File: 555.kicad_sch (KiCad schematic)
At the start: 57 parts, among them J2 Screw_Terminal_01x02, P1 USB_C_Plug_USB2.0, SW1 SW_Push, SW2 SW_Push, SW3 SW_Push, SW4 SW_Push, SW5 SW_Push, SW6 SW_Push, SW7 SW_Push, SW8 SW_Push, U1 NE555P

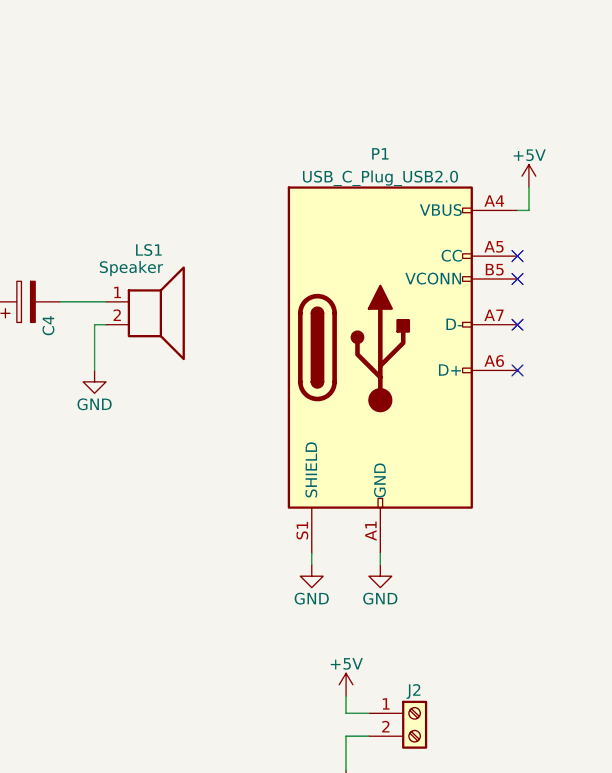
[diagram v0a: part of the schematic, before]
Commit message: USB-C resistor CC
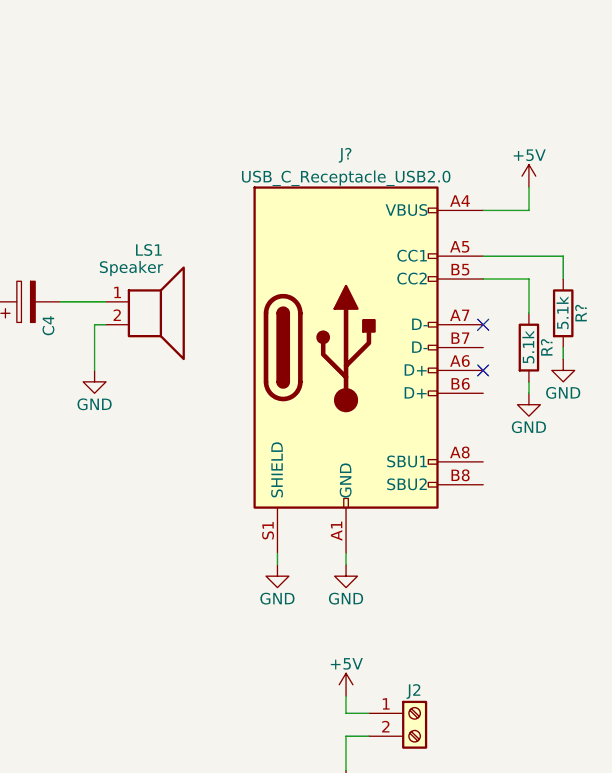
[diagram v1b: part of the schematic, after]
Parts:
- removed P1: USB_C_Plug_USB2.0, Connector_USB:USB_C_Receptacle_GCT_USB4085, symbol Connector:USB_C_Plug_USB2.0
- added J?: USB_C_Receptacle_USB2.0, symbol Connector:USB_C_Receptacle_USB2.0
- added R? (x2): 5.1k, Resistor_THT:R_Axial_DIN0207_L6.3mm_D2.5mm_P10.16mm_Horizontal, symbol Device:R
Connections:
- net +5V: now also J?.A4 (VBUS), J?.A9 (VBUS), J?.B4 (VBUS), J?.B9 (VBUS)
- net GND: now also J?.A1 (GND), J?.A12 (GND), J?.B1 (GND), J?.B12 (GND), J?.S1 (SHIELD), R?.2, R?.2
- new net: J?.B5 (CC2), R?.1
- new net: J?.A5 (CC1), R?.1
- no-connect marks 4 -> 2

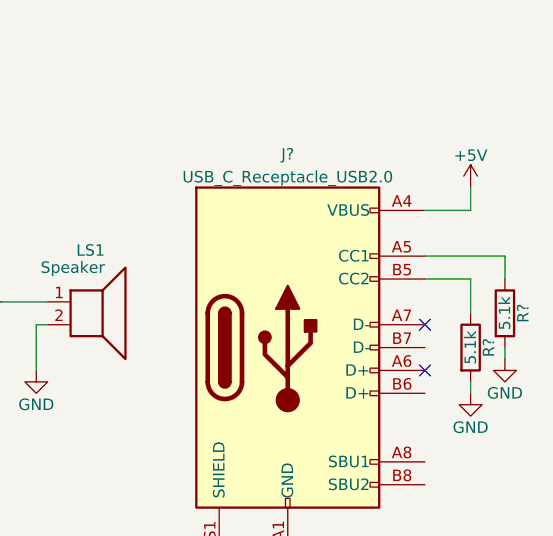
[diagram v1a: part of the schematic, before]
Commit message: USB-C resistor CC
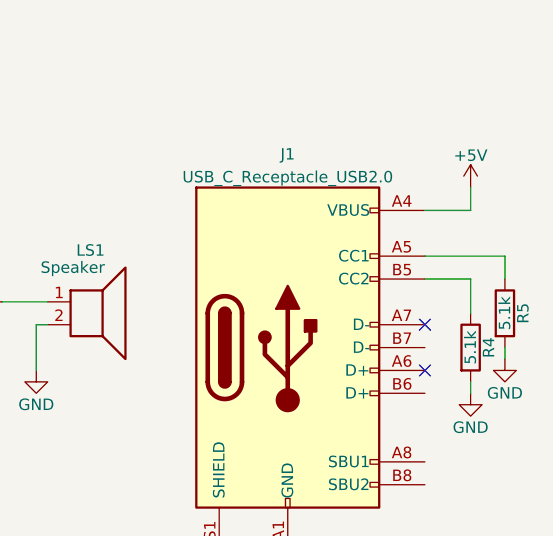
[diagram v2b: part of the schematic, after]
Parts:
- J1: renamed from J?; footprint (none) -> Connector_USB:USB_C_Receptacle_GCT_USB4085
- gave numbers to parts that had none: 2
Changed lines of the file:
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@@
   (symbol (lib_id "Device:R") (at 278.13 97.79 0) (unit 1)
     (in_bom yes) (on_board yes)
-    (property "Reference" "R?" (id 0) (at 280.162 97.79 90))
+    (property "Reference" "R4" (id 0) (at 280.162 97.79 90))
     (property "Value" "5.1k" (id 1) (at 278.13 97.79 90))
     (property "Footprint" "Resistor_THT:R_Axial_DIN0207_L6.3mm_D2.5mm_P10.16mm_Horizontal" (id 2) (at 276.352 97.79 90)
@@
   (symbol (lib_id "Device:R") (at 281.94 93.98 0) (unit 1)
     (in_bom yes) (on_board yes)
-    (property "Reference" "R?" (id 0) (at 283.972 93.98 90))
+    (property "Reference" "R5" (id 0) (at 283.972 93.98 90))
     (property "Value" "5.1k" (id 1) (at 281.94 93.98 90))
     (property "Footprint" "Resistor_THT:R_Axial_DIN0207_L6.3mm_D2.5mm_P10.16mm_Horizontal" (id 2) (at 280.162 93.98 90)
@@
   (symbol (lib_id "power:GND") (at 281.94 99.06 0) (unit 1)
     (in_bom yes) (on_board yes)
-    (property "Reference" "#PWR?" (id 0) (at 281.94 105.41 0)
+    (property "Reference" "#PWR0105" (id 0) (at 281.94 105.41 0)
       (effects (font (size 1.27 1.27)) hide)
     )
@@
   (symbol (lib_id "power:GND") (at 278.13 102.87 0) (unit 1)
     (in_bom yes) (on_board yes)
-    (property "Reference" "#PWR?" (id 0) (at 278.13 109.22 0)
+    (property "Reference" "#PWR0104" (id 0) (at 278.13 109.22 0)
       (effects (font (size 1.27 1.27)) hide)
     )
@@
   (symbol (lib_id "Connector:USB_C_Receptacle_USB2.0") (at 257.81 97.79 0) (unit 1)
     (in_bom yes) (on_board yes) (fields_autoplaced)
-    (property "Reference" "J?" (id 0) (at 257.81 76.3102 0))
+    (property "Reference" "J1" (id 0) (at 257.81 76.3102 0))
     (property "Value" "USB_C_Receptacle_USB2.0" (id 1) (at 257.81 78.8471 0))
-    (property "Footprint" "" (id 2) (at 261.62 97.79 0)
+    (property "Footprint" "Connector_USB:USB_C_Receptacle_GCT_USB4085" (id 2) (at 261.62 97.79 0)
       (effects (font (size 1.27 1.27)) hide)
     )
@@
       (reference "#PWR0103") (unit 1) (value "GND") (footprint "")
     )
+    (path "/b2e6477c-ad92-49a7-aece-eea1bc30ca39"
+      (reference "#PWR0104") (unit 1) (value "GND") (footprint "")
+    )
+    (path "/7a7afcf7-9c2f-4d82-ae0b-cb669e335a64"
+      (reference "#PWR0105") (unit 1) (value "GND") (footprint "")
+    )
     (path "/43a05453-035c-453b-be11-f0c5789d3e42"
       (reference "#PWR0106") (unit 1) (value "GND") (footprint "")
@@
       (reference "#PWR0108") (unit 1) (value "+5V") (footprint "")
     )
-    (path "/7a7afcf7-9c2f-4d82-ae0b-cb669e335a64"
-      (reference "#PWR?") (unit 1) (value "GND") (footprint "")
-    )
-    (path "/b2e6477c-ad92-49a7-aece-eea1bc30ca39"
-      (reference "#PWR?") (unit 1) (value "GND") (footprint "")
-    )
     (path "/f94bea49-4652-41d4-bccc-fb87f892bbde"
       (reference "C1") (unit 1) (value "10uF") (footprint "Capacitor_THT:CP_Radial_D5.0mm_P2.00mm")
@@
       (reference "D2") (unit 1) (value "LED") (footprint "LED_THT:LED_D5.0mm")
     )
+    (path "/da6fb2fe-a3cd-40a0-87c3-86aa919378d2"
+      (reference "J1") (unit 1) (value "USB_C_Receptacle_USB2.0") (footprint "Connector_USB:USB_C_Receptacle_GCT_USB4085")
+    )
     (path "/bd0631f4-de16-4346-98de-2fce907e4abe"
       (reference "J2") (unit 1) (value "Screw_Terminal_01x02") (footprint "TerminalBlock_Phoenix:TerminalBlock_Phoenix_PT-1,5-2-5.0-H_1x02_P5.00mm_Horizontal")
     )
-    (path "/da6fb2fe-a3cd-40a0-87c3-86aa919378d2"
-      (reference "J?") (unit 1) (value "USB_C_Receptacle_USB2.0") (footprint "")
-    )
     (path "/bc0347ee-e81a-4fa5-bb35-374b2cb74098"
       (reference "LS1") (unit 1) (value "Speaker") (footprint "TerminalBlock_Phoenix:TerminalBlock_Phoenix_PT-1,5-2-5.0-H_1x02_P5.00mm_Horizontal")
@@
       (reference "R3") (unit 1) (value "220") (footprint "Resistor_THT:R_Axial_DIN0207_L6.3mm_D2.5mm_P10.16mm_Horizontal")
     )
+    (path "/00fa8944-2b1f-4fa9-9017-80514ec84070"
+      (reference "R4") (unit 1) (value "5.1k") (footprint "Resistor_THT:R_Axial_DIN0207_L6.3mm_D2.5mm_P10.16mm_Horizontal")
+    )
+    (path "/18ab6926-aa6b-49c0-a18b-1f23dc112c2e"
+      (reference "R5") (unit 1) (value "5.1k") (footprint "Resistor_THT:R_Axial_DIN0207_L6.3mm_D2.5mm_P10.16mm_Horizontal")
+    )
     (path "/d88ab312-febf-4aef-8f6e-4613f011a683"
       (reference "R10") (unit 1) (value "2k") (footprint "Resistor_THT:R_Axial_DIN0207_L6.3mm_D2.5mm_P10.16mm_Horizontal")
@@
       (reference "R56") (unit 1) (value "1k") (footprint "Resistor_SMD:R_0201_0603Metric")
     )
-    (path "/00fa8944-2b1f-4fa9-9017-80514ec84070"
-      (reference "R?") (unit 1) (value "5.1k") (footprint "Resistor_THT:R_Axial_DIN0207_L6.3mm_D2.5mm_P10.16mm_Horizontal")
-    )
-    (path "/18ab6926-aa6b-49c0-a18b-1f23dc112c2e"
-      (reference "R?") (unit 1) (value "5.1k") (footprint "Resistor_THT:R_Axial_DIN0207_L6.3mm_D2.5mm_P10.16mm_Horizontal")
-    )
     (path "/eda38263-0621-4cb0-935b-348e3dbcbc4c"

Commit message: Art contribution AML
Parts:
- C1: value 10uF -> 1uF
- RV1: value 10k -> 20k
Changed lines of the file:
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@@
     (in_bom yes) (on_board yes)
     (property "Reference" "RV1" (id 0) (at 125.73 108.585 90))
-    (property "Value" "10k" (id 1) (at 125.73 106.68 90))
+    (property "Value" "20k" (id 1) (at 125.73 106.68 90))
     (property "Footprint" "Potentiometer_THT:Potentiometer_TT_P0915N" (id 2) (at 125.73 104.14 0)
       (effects (font (size 1.27 1.27)) hide)
@@
       (effects (font (size 1.27 1.27)) (justify left))
     )
-    (property "Value" "10uF" (id 1) (at 132.08 113.665 0)
+    (property "Value" "1uF" (id 1) (at 132.08 113.665 0)
       (effects (font (size 1.27 1.27)) (justify left))
     )
@@
     )
     (path "/f94bea49-4652-41d4-bccc-fb87f892bbde"
-      (reference "C1") (unit 1) (value "10uF") (footprint "Capacitor_THT:CP_Radial_D5.0mm_P2.00mm")
+      (reference "C1") (unit 1) (value "1uF") (footprint "Capacitor_THT:CP_Radial_D5.0mm_P2.00mm")
     )
     (path "/647969e2-18be-4c4f-a5bd-0b278ed920c4"
@@
     )
     (path "/eda38263-0621-4cb0-935b-348e3dbcbc4c"
-      (reference "RV1") (unit 1) (value "10k") (footprint "Potentiometer_THT:Potentiometer_TT_P0915N")
+      (reference "RV1") (unit 1) (value "20k") (footprint "Potentiometer_THT:Potentiometer_TT_P0915N")
     )
     (path "/6e101411-4ba4-4c62-be46-5c987ad8894a"
